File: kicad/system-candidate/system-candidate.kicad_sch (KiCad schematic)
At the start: 76 parts, among them J1 691137710002 2P 5.00mm, J2 Auxiliary 12V, J3 Differential audio, J4 Control 2x4: 3V3 RESET FAULT 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, J5 691137710002 2P 5.00mm, J6 GND braid solder bond - NO mo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, U1 TPA3255DDV, U2 OPA1656ID, U3 OPA1656ID

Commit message: feat(eda): capture discrete D-020 sequencer and integrate D-021 power into system candidate
- seq-d020 (D-023): LP2985 3.3 V, two TPS3808 stages (>=360 ms hold),
  74LVC2G74 RUN/ARMED latches (human start edge with CLIP_OTW high, FAULT
  arming and latch with human re-arm), 0.62-1.44 s start timeout, TPS3700
  windows for ANALOG_12V and VMID on the RAILS_OK wired-AND.
- seq_d020_logic simulates the captured netlist; mutation-checked tests.
- system-candidate: power and seq banks outside the OEM outline, 150
  footprints, 421 native pins matched; PVDD_36V renamed PVDD; J4/R7/R8 DNP.
  ERC equal to base (4 PBTL OUT_x, 1 MONO_BIASED), DRC 0, 338 unrouted.
- power-d021: candidate stock footprints, SEQ_3V3 pull-up, manifest restored.
- 3D gallery adds system candidate views framed to show import banks.
- D-019 isolation, discharge, DC sense and mute remain NOT implemented.
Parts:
- added C301, C302: 4700u 63V, Capacitor_THT:CP_Radial_D25.0mm_P10.00mm_SnapIn, symbol Device:C_Polarized
- added C310, C311: 2.2u 100V X7R, Capacitor_SMD:C_1210_3225Metric, symbol Device:C
- added C312: 2.2n 50V X7R, Capacitor_SMD:C_0402_1005Metric, symbol Device:C
- added C313: 3.3n, Capacitor_SMD:C_0603_1608Metric, symbol Device:C
- added C314: 56p, Capacitor_SMD:C_0603_1608Metric, symbol Device:C
- added C315, C316: 22u 25V X7R, Capacitor_SMD:C_1210_3225Metric, symbol Device:C
- added C320, C406, C407, C408, C409, C410, C411, C412, C413, C414, C415, C416, C417: 100n, Capacitor_SMD:C_0603_1608Metric, symbol Device:C
- added C401: 1u 25V, Capacitor_SMD:C_0603_1608Metric, symbol Device:C
- added C402: 10n, Capacitor_SMD:C_0603_1608Metric, symbol Device:C
- added C403: 2.2u 10V, Capacitor_SMD:C_0603_1608Metric, symbol Device:C
- added C404: 180n, Capacitor_SMD:C_0603_1608Metric, symbol Device:C
- added C405: 1u, Capacitor_SMD:C_0603_1608Metric, symbol Device:C
- added D301, D302: RECT >=400V, Diode_THT:D_P600_R-6_P12.70mm_Horizontal, symbol Device:D
- added D303: TVS VWM>=51V, Diode_SMD:D_SMC, symbol Device:D_TVS
- added F301: T8A slow, Fuse:Fuseholder_Cylinder-5x20mm_Schurter_0031_8201_Horizontal_Open, symbol Device:Fuse
- added J301: T1_SECONDARY, Connector_JST:JST_VH_B3P-VH_1x03_P3.96mm_Vertical, symbol Connector_Generic:Conn_01x03
- added J401: START_BUTTON, Connector_PinHeader_2.54mm:PinHeader_1x02_P2.54mm_Vertical, symbol Connector_Generic:Conn_01x02
- added L301: 68u, Inductor_SMD:L_Coilcraft_MSS1246T-XXX, symbol Device:L
- added R301: 4.7k 2W, Resistor_THT:R_Axial_DIN0414_L11.9mm_D4.5mm_P15.24mm_Horizontal, symbol Device:R
- added R310: 100k 1%, Resistor_SMD:R_0603_1608Metric, symbol Device:R
- added R311, R313: 453k 1%, Resistor_SMD:R_0603_1608Metric, symbol Device:R
- added R312: 49.9k 1%, Resistor_SMD:R_0603_1608Metric, symbol Device:R
- added R320: 931k 0.1%, Resistor_SMD:R_1206_3216Metric, symbol Device:R
- added R321: 6.04k 0.1%, Resistor_SMD:R_0603_1608Metric, symbol Device:R
- added R322: 7.32k 0.1%, Resistor_SMD:R_0603_1608Metric, symbol Device:R
- added R323, R401, R402, R403, R404, R405, R406: 100k, Resistor_SMD:R_0603_1608Metric, symbol Device:R
- added R407: 10k, Resistor_SMD:R_0603_1608Metric, symbol Device:R
- added R408: 1k, Resistor_SMD:R_0603_1608Metric, symbol Device:R
- added R420, R422, R426: 1M, Resistor_SMD:R_0603_1608Metric, symbol Device:R
- added R421: 46.4k, Resistor_SMD:R_0603_1608Metric, symbol Device:R
- added R423: 30.1k, Resistor_SMD:R_0603_1608Metric, symbol Device:R
- added R424: 909k, Resistor_SMD:R_0603_1608Metric, symbol Device:R
- added R425: 101k, Resistor_SMD:R_0603_1608Metric, symbol Device:R
- added R427: 64.9k, Resistor_SMD:R_0603_1608Metric, symbol Device:R
- added U302: LM5164DDA, Package_SO:HSOP-8-1EP_3.9x4.9mm_P1.27mm_EP2.41x3.1mm, symbol Regulator_Switching:LM5164DDA
- added U303, U412, U413: TPS3700DDC, Package_TO_SOT_SMD:SOT-23-6, symbol PS28_POWER:TPS3700DDC
- added U401: LP2985-33, Package_TO_SOT_SMD:SOT-23-5, symbol PS28_SEQ:LP2985-33DBV
- added U402, U403, U404: TPS3808G33, Package_TO_SOT_SMD:SOT-23-6, symbol Power_Supervisor:TPS3808DBV
- added U405: 74LVC1G14, Package_TO_SOT_SMD:SOT-23-5, symbol 74xGxx:74LVC1G14
- added U406, U407: 74LVC2G74, Package_SO:SSOP-8_2.95x2.8mm_P0.65mm, symbol 74xGxx:74LVC2G74
- added U408: 74LVC1G32, Package_TO_SOT_SMD:SOT-23-5, symbol 74xGxx:74LVC1G32
- added U409: 74LVC1G07, Package_TO_SOT_SMD:SOT-23-5, symbol 74xGxx:74LVC1G07
- added U410: 74LVC1G08, Package_TO_SOT_SMD:SOT-23-5, symbol 74xGxx:74LVC1G08
- added U411: 74LVC1G06, Package_TO_SOT_SMD:SOT-23-5, symbol 74xGxx:74LVC1G06
- J4, R7, R8: now not fitted
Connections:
- net ANALOG_12V: now also R420.1, R422.1
- net AUX_RAW: now also C313.2, C315.1, C316.1, C320.1, C401.1, C416.1, C417.1, L301.2, R311.1, U303.5 (VDD), U401.1 (VIN), U401.3 (ON/OFF), U412.5 (VDD), U413.5 (VDD)
- net CLIP_OTW: now also U406.2 (D)
- net FAULT: now also U407.1 (C), U408.2
- net GND: now also C301.2, C302.2, C310.2, C311.2, C315.2, C316.2, C320.2, C401.2, C402.2, C403.2, C404.2, C405.2, C406.2, C407.2, C408.2, C409.2, C410.2, C411.2, C412.2, C413.2, C414.2, C415.2, C416.2, C417.2, D303.2 (A2), F301.2, J401.2 (Pin_2), R301.2, R310.2, R312.2, R322.2, R421.2, R423.2, R425.2, R427.2, U302.1 (GND), U302.9 (EP), U303.2 (GND), U401.2 (GND), U402.2 (GND), U403.2 (GND), U404.2 (GND), U405.3 (GND), U406.4 (GND), U407.4 (GND), U408.3 (GND), U409.3 (GND), U410.3 (GND), U411.3 (GND), U412.2 (GND), U413.2 (GND)
- net RESET: now also R408.2
- net VMID: now also R424.1, R426.1
- net PVDD_36V renamed PVDD
- net PVDD: now also C301.1, C302.1, C310.1, C311.1, D301.1 (K), D302.1 (K), D303.1 (A1), R301.1, R320.1, U302.2 (VIN), U302.3 (EN/UVLO)
- new net ANALOG_OV: R422.2, R423.1, U412.4 (INB-)
- new net ANALOG_UV: R420.2, R421.1, U412.3 (INA+)
- new net BUCK_BST: C312.1, U302.7 (BST)
- new net BUCK_FB: C314.2, R311.2, R312.1, U302.5 (FB)
- new net BUCK_RAMP: C313.1, C314.1, R313.2
- new net BUCK_RON: R310.1, U302.4 (RON)
- new net BUCK_SW: C312.2, L301.1, R313.1, U302.8 (SW)
- new net FAULT_TRIP_N: U408.4, U409.2
- new net NOT_ARMED: U407.3 (~{Q}), U408.1, U410.2
- new net PVDD_OV_SENSE: R321.2, R322.1, U303.4 (INB-)
- new net PVDD_UV_SENSE: R320.2, R321.1, U303.3 (INA+)
- new net RAILS_OK: R323.2, U302.6 (PGOOD), U303.1 (OUTA), U303.6 (OUTB), U402.3 (~{MR}), U409.4, U411.4, U412.1 (OUTA), U412.6 (OUTB), U413.1 (OUTA), U413.6 (OUTB)
- new net RAILS_QUAL: R404.2, U403.1 (~{RESET}), U406.6 (~{CLR})
- new net RUN: R408.1, U406.5 (Q), U407.2 (D), U407.6 (~{CLR}), U410.1
- new net SEQ_3V3: C403.1, C406.1, C407.1, C408.1, C409.1, C410.1, C411.1, C412.1, C413.1, C414.1, C415.1, R323.1, R401.1, R402.1, R403.1, R404.1, R405.1, R406.1, U401.5 (VOUT), U402.5 (SENSE), U402.6 (VDD), U403.5 (SENSE), U403.6 (VDD), U404.5 (SENSE), U404.6 (VDD), U405.5 (VCC), U406.7 (~{PRE}), U406.8 (VCC), U407.7 (~{PRE}), U407.8 (VCC), U408.5 (VCC), U409.5 (VCC), U410.5 (VCC), U411.5 (VCC)
- new net SEQ_BYP: C402.1, U401.4 (BYPASS)
- new net SEQ_CT1: R401.2, U402.4 (CT)
- new net SEQ_CT2: R403.2, U403.4 (CT)
- new net SEQ_CT3: C404.1, U404.4 (CT)
- new net SEQ_HOLD1: R402.2, U402.1 (~{RESET}), U403.3 (~{MR})
- new net START_BTN: J401.1 (Pin_1), R406.2, R407.1
- new net START_DEB: C405.1, R407.2, U405.2
- new net START_EDGE: U405.4, U406.1 (C)
- new net START_TIMEOUT: R405.2, U404.1 (~{RESET}), U411.2
- new net START_WIN: U404.3 (~{MR}), U410.4
- new net T1_A: D301.2 (A), J301.1 (Pin_1)
- new net T1_B: D302.2 (A), J301.3 (Pin_3)
- new net T1_CT: F301.1, J301.2 (Pin_2)
- new net VMID_OV: R426.2, R427.1, U413.4 (INB-)
- new net VMID_UV: R424.2, R425.1, U413.3 (INA+)
- no-connect marks 4 -> 8
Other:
- note added: "D-020 DISCRETE SUBSET: NO ISOLATION/DISCHARGE/DC/MUTE (D-019 OPEN)"
- note added: "D-021 POWER: FOOTPRINTS NOT AUDITED; NEVER BRIDGE T1_A-T1_B"
- title: PS28 CORE + PROTECTED ANALOG - INCOMPLETE SAFETY REVIEW CANDIDATE -> PS28 CORE + ANALOG + D-021 POWER + D-020 SEQ SUBSET - INCOMPLETE SAFETY REVIEW

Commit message: feat(eda): complete D-019 input interface with Form C relay, mute and DC observation
- iso-d019 (D-024): Omron G6K-2F DC12 after C20/C21 (COM isolated plate,
  NO TPA pin, NC 1k discharge; break-before-make, isolated when unpowered),
  TMUX6219 mute DIVIDED->VMID, TPS3700 DC windows on both pins (2-5 V,
  tau ~50 ms) and AUX_RAW window, MMBT3904 relay/mute drivers.
- seq-d020: RESET released 12-28 ms after relay command, DC dwell 12-28 ms
  before AUDIO_EN latch, DC loss trips RAILS_OK, start timeout covers dwell.
- simulate_d019: 1350 ngspice cases, pin -0.262..6.61 V within -0.3..7 V
  (worst with pessimistic 10 ms opening; >= 0 V at datasheet 3 ms).
- system-candidate: 200 footprints, 570 pins matched, bridge closed only
  via K501, J3 DNP; ERC equal to base, DRC 0, 464 unrouted.
- Not covered: single-fault preamp rail/driver short, real TPA input when
  unpowered, contact bounce/stuck, content below 20 Hz.
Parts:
- added C418, C419, C420, C421, C422, C423, C505, C506, C507, C508: 100n, Capacitor_SMD:C_0603_1608Metric, symbol Device:C
- added C503, C504: 4.7n C0G, Capacitor_SMD:C_0603_1608Metric, symbol Device:C
- added C509, C511: 330n, Capacitor_SMD:C_0603_1608Metric, symbol Device:C
- added C510, C512: 680n, Capacitor_SMD:C_0603_1608Metric, symbol Device:C
- added D501: 1N4148W, Diode_SMD:D_SOD-123, symbol Device:D
- added D502: BZT52C15, Diode_SMD:D_SOD-123, symbol Device:D_Zener
- added K501: G6K-2F DC12, Relay_SMD:Relay_DPDT_Omron_G6K-2F, symbol Relay:G6K-2
- added Q501, Q502: MMBT3904, Package_TO_SOT_SMD:SOT-23, symbol PS28_ISO:MMBT3904
- added R428, R429, R430, R502, R511, R513: 100k, Resistor_SMD:R_0603_1608Metric, symbol Device:R
- added R501: 2.2k, Resistor_SMD:R_0603_1608Metric, symbol Device:R
- added R503, R504: 1k, Resistor_SMD:R_0603_1608Metric, symbol Device:R
- added R505, R508: 787k, Resistor_SMD:R_0603_1608Metric, symbol Device:R
- added R506, R509: 115k, Resistor_SMD:R_0603_1608Metric, symbol Device:R
- added R507, R510: 78.7k, Resistor_SMD:R_0603_1608Metric, symbol Device:R
- added R512: 10k, Resistor_SMD:R_0603_1608Metric, symbol Device:R
- added R514: 357k, Resistor_SMD:R_0603_1608Metric, symbol Device:R
- added R515: 1.5k, Resistor_SMD:R_0603_1608Metric, symbol Device:R
- added R516: 11.5k, Resistor_SMD:R_0603_1608Metric, symbol Device:R
- added U414, U416: TPS3808G33, Package_TO_SOT_SMD:SOT-23-6, symbol Power_Supervisor:TPS3808DBV
- added U415: 74LVC1G08, Package_TO_SOT_SMD:SOT-23-5, symbol 74xGxx:74LVC1G08
- added U417: 74LVC2G74, Package_SO:SSOP-8_2.95x2.8mm_P0.65mm, symbol 74xGxx:74LVC2G74
- added U418: 74LVC1G32, Package_TO_SOT_SMD:SOT-23-5, symbol 74xGxx:74LVC1G32
- added U419: 74LVC1G07, Package_TO_SOT_SMD:SOT-23-5, symbol 74xGxx:74LVC1G07
- added U501, U502, U504: TPS3700DDC, Package_TO_SOT_SMD:SOT-23-6, symbol PS28_POWER:TPS3700DDC
- added U503: TMUX6219, Package_SO:MSOP-8_3x3mm_P0.65mm, symbol PS28_ISO:TMUX6219DGK
- J3: now not fitted
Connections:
- net DIFF_NEG is gone; now on net DIFF_N: R108.1, U3.7
- net DIFF_POS is gone; now on net DIFF_P: C104.2, C105.2, R107.1, U3.1, U3.2 (-)
- net ANALOG_12V: now also C505.1, R511.1, U503.4 (VDD)
- net AUX_RAW: now also C506.1, C507.1, C508.1, D502.2 (A), K501.1, R514.1, U501.5 (VDD), U502.5 (VDD), U504.5 (VDD)
- net DIVIDED: now also U503.1 (D)
- net GND: now also C418.2, C419.2, C420.2, C421.2, C422.2, C423.2, C503.2, C504.2, C505.2, C506.2, C507.2, C508.2, C509.2, C510.2, C511.2, C512.2, Q501.2 (E), Q502.2 (E), R502.2, R503.2, R504.2, R507.2, R510.2, R513.2, R516.2, U414.2 (GND), U415.3 (GND), U416.2 (GND), U417.4 (GND), U418.3 (GND), U419.3 (GND), U501.2 (GND), U502.2 (GND), U503.3 (GND), U503.6 (SEL), U503.7 (VSS), U503.8 (S2), U504.2 (GND)
- net INPUT_A_AC: now also C503.1, K501.4, R505.1; no longer C20.2
- net INPUT_B_AC: now also C504.1, K501.5, R508.1; no longer C21.2
- net NOT_ARMED: no longer U410.2
- net RAILS_OK: now also U419.4, U504.1 (OUTA), U504.6 (OUTB)
- net RUN: now also R501.1, U414.3 (~{MR}), U417.6 (~{CLR}); no longer R408.1
- net SEQ_3V3: now also C418.1, C419.1, C420.1, C421.1, C422.1, C423.1, R428.1, R429.1, R430.1, U414.5 (SENSE), U414.6 (VDD), U415.5 (VCC), U416.5 (SENSE), U416.6 (VDD), U417.2 (D), U417.7 (~{PRE}), U417.8 (VCC), U418.5 (VCC), U419.5 (VCC)
- net VMID: now also U503.2 (S1)
- net ARMED: now reaches U407.5 (Q)
- net ARMED: now also U415.1
- new net AUDIO_EN: R512.1, U417.5 (Q)
- new net AUX_OV: R515.2, R516.1, U504.4 (INB-)
- new net AUX_UV: R514.2, R515.1, U504.3 (INA+)
- new net DC_GATE: U415.4, U416.3 (~{MR})
- new net DC_OK: R429.2, U415.2, U418.2, U501.1 (OUTA), U501.6 (OUTB), U502.1 (OUTA), U502.6 (OUTB)
- new net DC_TRIP_N: U418.4, U419.2
- new net DWELL_OK: R430.2, U416.1 (~{RESET}), U417.1 (C)
- new net INA_DIS: K501.2, R503.1
- new net INA_ISO: C20.2, K501.3
- new net INA_OV: C510.1, R506.2, R507.1, U501.4 (INB-)
- new net INA_UV: C509.1, R505.2, R506.1, U501.3 (INA+)
- new net INB_DIS: K501.7, R504.1
- new net INB_ISO: C21.2, K501.6
- new net INB_OV: C512.1, R509.2, R510.1, U502.4 (INB-)
- new net INB_UV: C511.1, R508.2, R509.1, U502.3 (INA+)
- new net MUTE_BASE: Q502.1 (B), R512.2, R513.1
- new net MUTE_EN: Q502.3 (C), R511.2, U503.5 (EN)
- new net NOT_AUDIO: U410.2, U417.3 (~{Q}), U418.1
- new net RELAY_BASE: Q501.1 (B), R501.2, R502.1
- new net RELAY_DRV: D501.2 (A), K501.8, Q501.3 (C)
- new net RELAY_FLY: D501.1 (K), D502.1 (K)
- new net RESET_GO: R408.1, R428.2, U414.1 (~{RESET})
- no-connect marks 8 -> 10
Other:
- note added: "D-020/D-024 DISCRETE SEQUENCER"
- note added: "D-024 INPUT ISOLATION RELAY / MUTE / DC WINDOWS"
- note added: "D-024: DRIVERS REACH TPA ONLY THROUGH RELAY K501 (iso-d019); DO NOT ENERGIZE"
- note removed: "D-019 OUTPUT BRIDGE OPEN: NO ISOLATION/MUTE/SUPERVISOR IMPLEMENTED; DO NOT ENERGIZE"
- note removed: "D-020 DISCRETE SUBSET: NO ISOLATION/DISCHARGE/DC/MUTE (D-019 OPEN)"
- moved on the sheet: C406, C407, C408, C409, C410, C411, C412, C413, C414, C415, C416, C417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

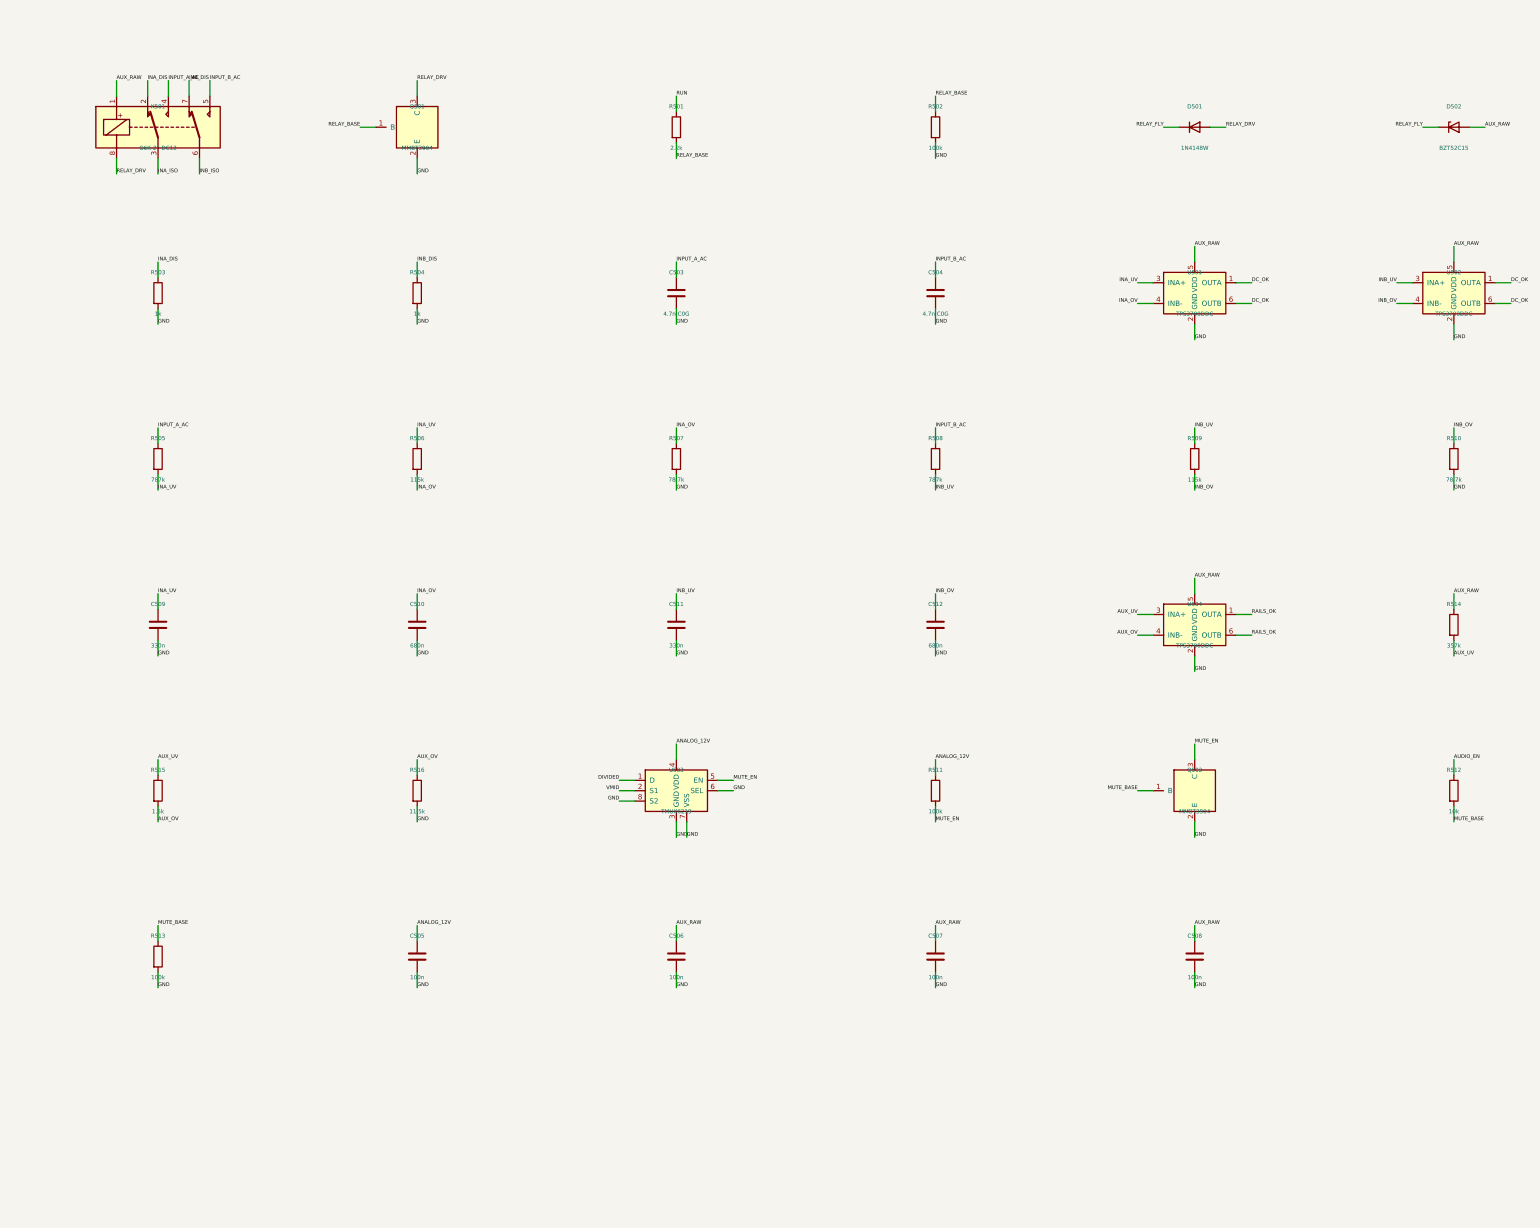
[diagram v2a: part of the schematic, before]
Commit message: feat(eda): clamp TPA inputs against single faults and audit TMUX6219 land pattern
- D-024a: 3.3k series after relay NO plus BAT54 (K on pin, A to GND).
  Driver shorted low with relay closed: about -5.9 V unclamped, <= -0.351 V
  at datasheet maximum VF (still 51 mV beyond -0.3 V); gain -1.33 dB typ.
- simulate_d019: 216 single-fault cases; normal cases now -0.158..6.47 V.
- Local TI DGK0008A footprint (SCDS420E p.50) replaces generic MSOP-8.
- Risk table in iso-d019.md: bounce resolved by design, sub-20 Hz fails
  safe, stuck-high driver and unpowered TPA input remain open.
- system-candidate: 204 footprints, 580 pins matched, DRC 0; gallery and
  SVG regenerated.
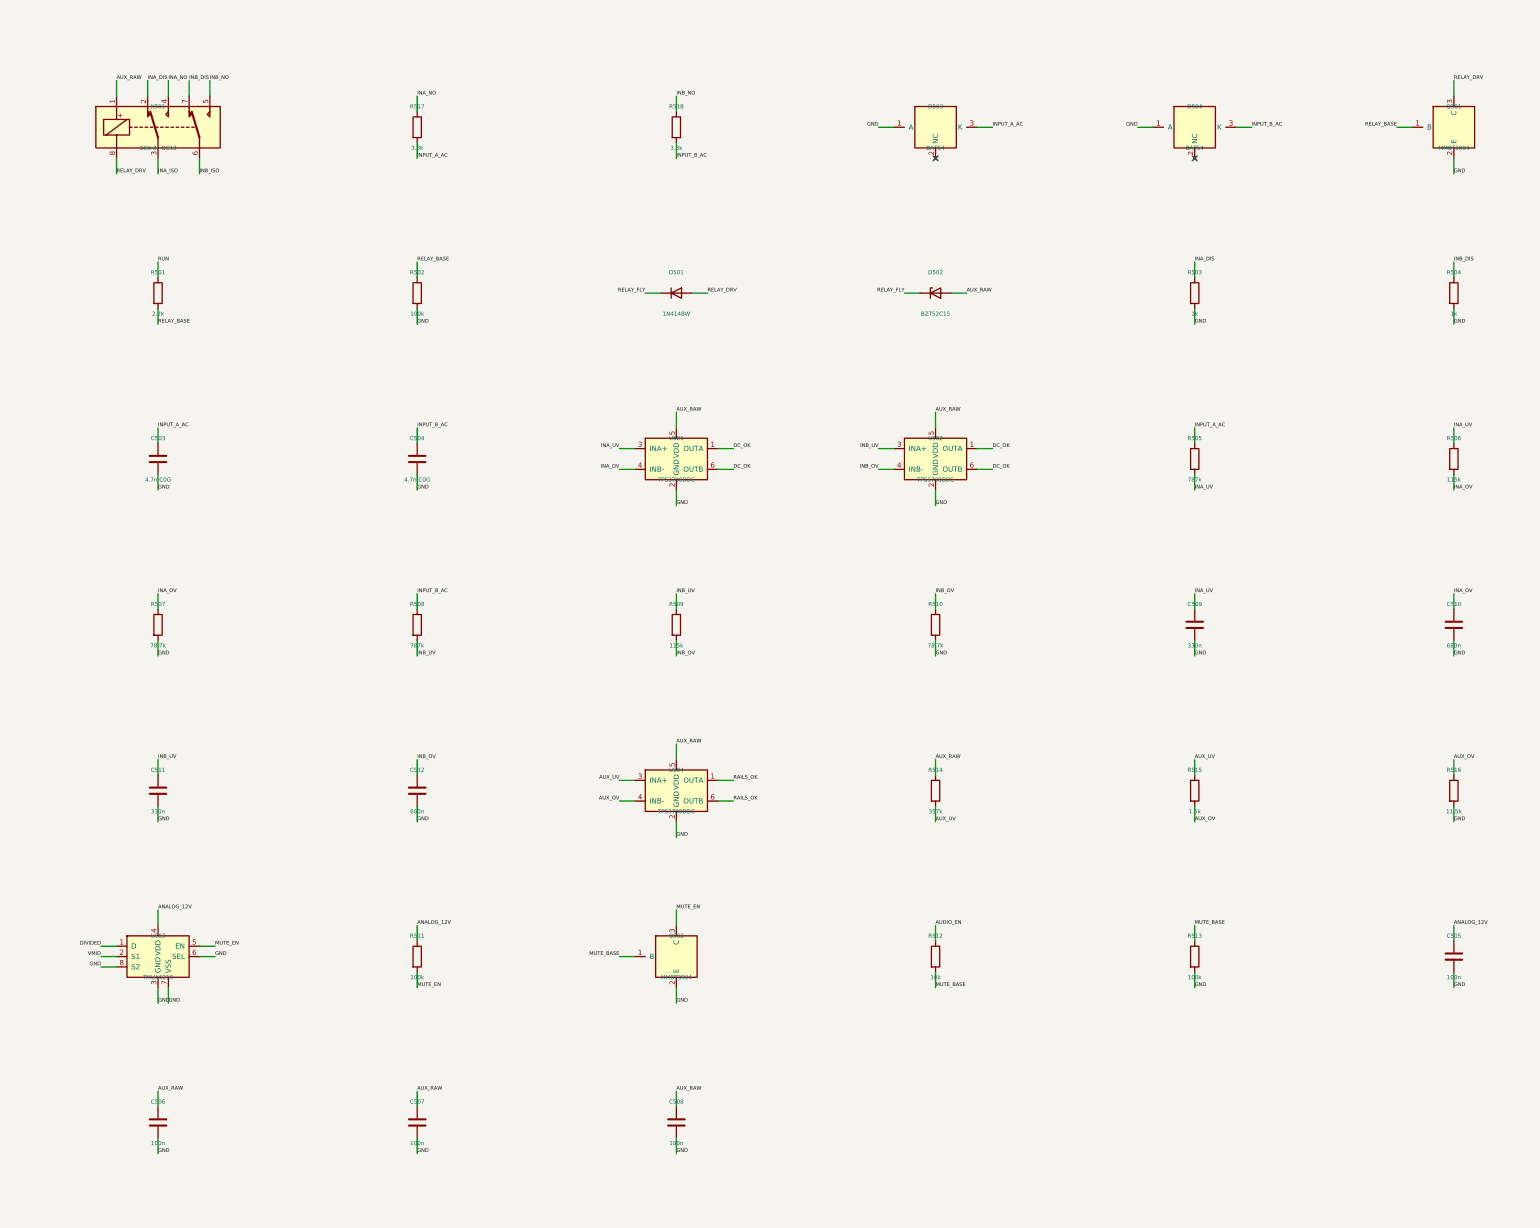
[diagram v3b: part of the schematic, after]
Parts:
- added D503, D504: BAT54, Package_TO_SOT_SMD:SOT-23, symbol PS28_ISO:BAT54
- added R517, R518: 3.3k, Resistor_SMD:R_0603_1608Metric, symbol Device:R
- U503: footprint Package_SO:MSOP-8_3x3mm_P0.65mm -> PS28_ANALOG:TI_DGK0008A
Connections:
- net GND: now also D503.1 (A), D504.1 (A)
- net INPUT_A_AC: now also D503.3 (K), R517.2; no longer K501.4
- net INPUT_B_AC: now also D504.3 (K), R518.2; no longer K501.5
- new net INA_NO: K501.4, R517.1
- new net INB_NO: K501.5, R518.1
- no-connect marks 10 -> 12
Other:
- moved on the sheet: C503, C504, C505, C506, C507, C508, C509, C510, C511, C512, D501, D502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

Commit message: varias ataulizaçoes e correçoes
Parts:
- C301, C302: value 4700u 63V -> 4700u 63V snap-in; MPN TBD: >=63 V, 105 C, ripple >=3.5 A at 120 Hz each -> Rubycon 63USC4700MEFCSN30X30 (LCSC C1498587): 4700 uF/63 V,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
- D301, D302: value RECT >=400V -> MUR3040WTG; MPN TBD: VRRM>=400 V, IF(AV)>=6 A, IFSM>=200 A -> onsemi MUR3040WTG (MUR3020WT/D Rev.7): VRRM 400 V, IF(AV) 1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
- D303: value TVS VWM>=51V -> SMCJ51A; MPN TBD: VWM>=51 V (above 49.8 V worst idle), Vc below 69 V abs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 -> Littelfuse SMCJ51A: VWM 51.0 V, Vc 82.4 V @IPP 18.2 A, PPP 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
- F301: value T8A slow -> T6.3A slow; MPN TBD: time-lag, I2t >= 60 A2s inrush margin, >=63 VDC -> Time-lag (T) 5x20 mm; I2t melt above measured inrush, >=63 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
- J301: MPN TBD: mate original T1 harness (3-way, red-black-red, ~3.96 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 -> JST VH SVH-41T-P1.1 terminals (20-16 AWG, 10 A) on VHR-4N h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
